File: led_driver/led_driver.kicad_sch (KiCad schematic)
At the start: 11 parts, among them J1 Conn_01x03_Male, J2 Screw_Terminal_01x06, Q1 IRFZ44N, Q2 IRFZ44N, Q3 IRFZ44N

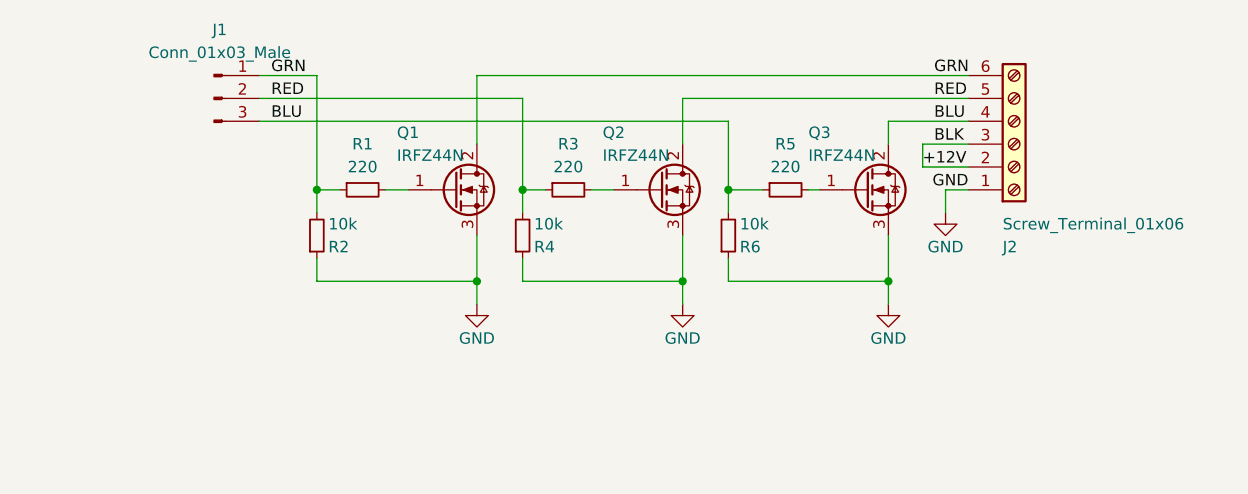
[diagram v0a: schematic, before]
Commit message: Tidy LED Driver schematic and print it to pdf
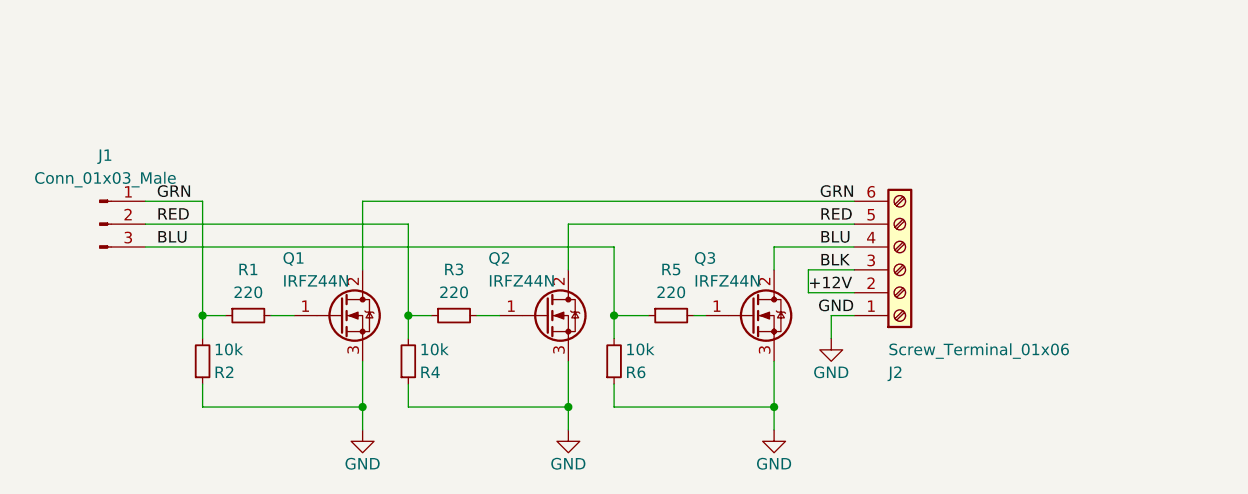
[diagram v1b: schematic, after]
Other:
- company: (none) -> Fridfinnur M, University of Iceland
- title: (none) -> LED Strip Driver for Robot Butler Project
- moved on the sheet: J1, J2, Q1, Q2, Q3, R1, R2, R3, R4, R5, R6
